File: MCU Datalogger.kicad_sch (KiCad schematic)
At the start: 0 parts

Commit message: Added required symbols to the schematic sheets.
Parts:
- added BT1: Battery, Connector_PinHeader_2.54mm:PinHeader_1x02_P2.54mm_Vertical, symbol Device:Battery
- added C1, C4: 0.1uF, Capacitor_SMD:C_0805_2012Metric, symbol Device:C
- added C2, C3: 22pF, Capacitor_SMD:C_0805_2012Metric, symbol Device:C
- added C5: 100nF, Capacitor_SMD:C_0805_2012Metric, symbol Device:C
- added D1, D2: LED, LED_SMD:LED_0805_2012Metric, symbol Device:LED
- added H1, H2, H3, H4: MountingHole, MountingHole:MountingHole_2.1mm, symbol Mechanical:MountingHole
- added J1, J3: Conn_01x04_Pin, Connector_PinHeader_2.54mm:PinHeader_1x04_P2.54mm_Vertical, symbol Connector:Conn_01x04_Pin
- added J2: Conn_01x09_Pin, Connector_PinHeader_2.54mm:PinHeader_1x09_P2.54mm_Vertical, symbol Connector:Conn_01x09_Pin
- added J4: Conn_02x03_Odd_Even, Connector_PinHeader_2.54mm:PinHeader_2x03_P2.54mm_Vertical, symbol Connector_Generic:Conn_02x03_Odd_Even
- added R1, R2, R6: 10K, Resistor_SMD:R_0805_2012Metric, symbol Device:R
- added R3, R4: 4.7K, Resistor_SMD:R_0805_2012Metric, symbol Device:R
- added R5, R7: 330, Resistor_SMD:R_0805_2012Metric, symbol Device:R
- added U1: DS1337S_, DS1337S_:SOIC127P600X175-8N, symbol DS1337S_:DS1337S_
- added U2, U3: 24LC1025, Package_SO:SOIC-8_5.3x5.3mm_P1.27mm, symbol Memory_EEPROM:24LC1025
- added U4: ATMEGA328P-AU, ATMEGA328P-AU:QFP80P900X900X120-32N, symbol ATMEGA328P-AU:ATMEGA328P-AU
- added Y1: 32.768 KHz, Crystal:Crystal_SMD_5032-2Pin_5.0x3.2mm_HandSoldering, symbol Device:Crystal
- added Y2: 16 MHz, Crystal:Crystal_SMD_5032-2Pin_5.0x3.2mm_HandSoldering, symbol Device:Crystal
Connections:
- new net GND: U4.21 (GND), U4.3 (GND), U4.5 (GND)
- new net VCC: U4.4 (VCC), U4.6 (VCC)
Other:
- title: (none) -> MCU Datalogger

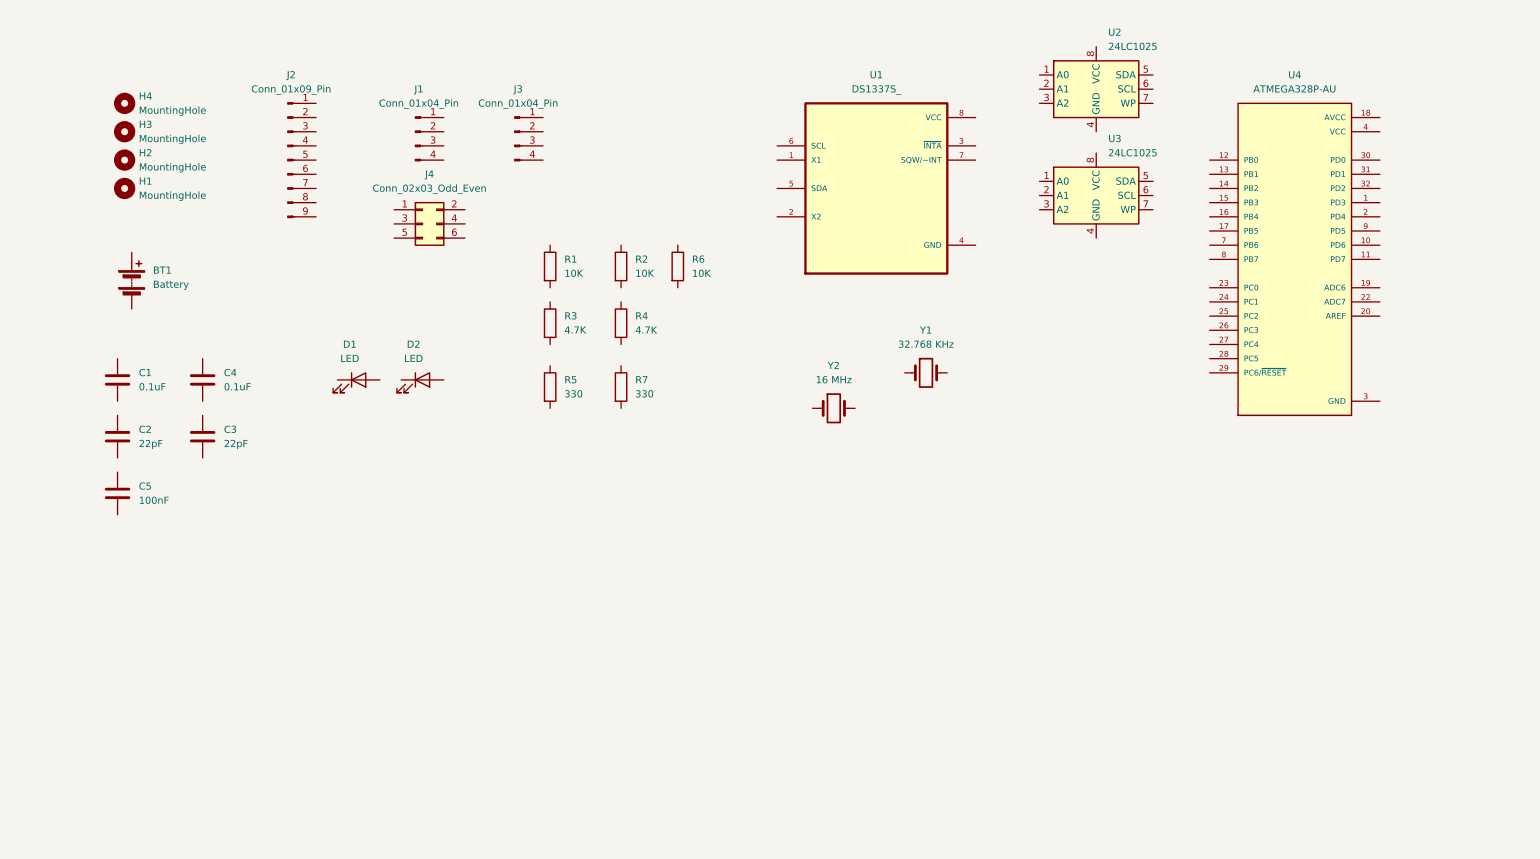
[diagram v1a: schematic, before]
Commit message: Completed wiring of main sheet.
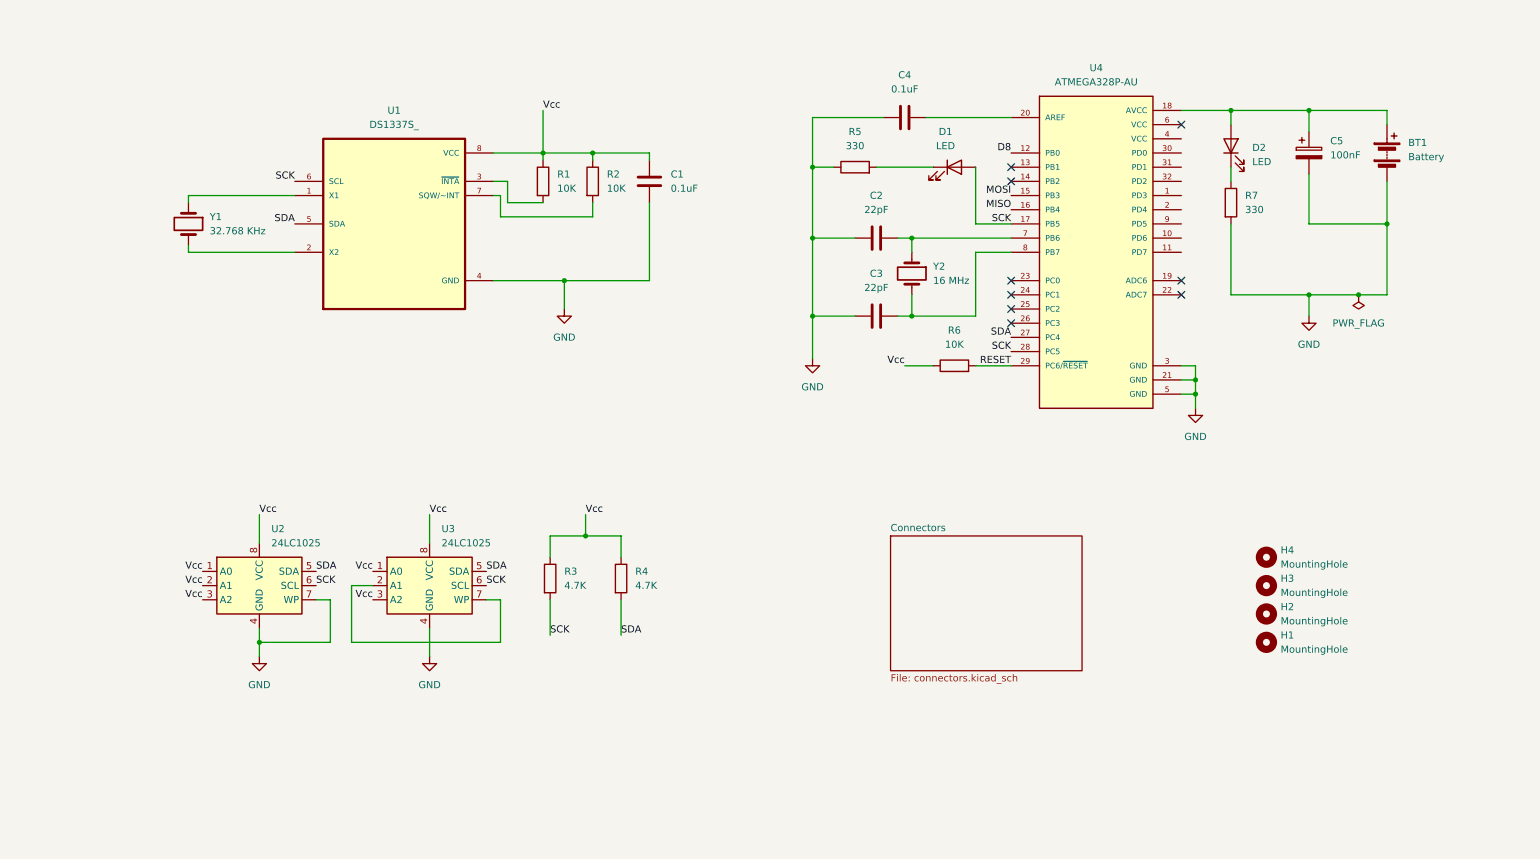
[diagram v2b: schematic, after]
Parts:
- removed J1, J3: Conn_01x04_Pin, Connector_PinHeader_2.54mm:PinHeader_1x04_P2.54mm_Vertical, symbol Connector:Conn_01x04_Pin
- removed J2: Conn_01x09_Pin, Connector_PinHeader_2.54mm:PinHeader_1x09_P2.54mm_Vertical, symbol Connector:Conn_01x09_Pin
- removed J4: Conn_02x03_Odd_Even, Connector_PinHeader_2.54mm:PinHeader_2x03_P2.54mm_Vertical, symbol Connector_Generic:Conn_02x03_Odd_Even
- C5: symbol Device:C -> Device:C_Polarized
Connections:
- net GND: now also BT1.2 (-), C1.2, C2.2, C3.2, C4.1, C5.2, R5.1, R7.2, U1.4 (GND), U2.4 (GND), U2.7 (WP), U3.4 (GND)
- net at R4.1: no longer names the net of R4.1
- net at R4.1: now also C1.1, R1.1, R2.1, R3.1, R6.1, U1.8 (VCC), U2.1 (A0), U2.2 (A1), U2.3 (A2), U2.8 (VCC), U3.1 (A0), U3.3 (A2), U3.8 (VCC)
- net SDA: now reaches R4.2
- net SDA: now also U1.5 (SDA), U2.5 (SDA), U3.5 (SDA), U4.27 (PC4)
- net at Y1.1: now also U1.1 (X1)
- net at Y1.2: now also U1.2 (X2)
- net RESET: now reaches R6.2
- net RESET: now also U4.29 (PC6/~{RESET})
- net at R5.2: now also D1.1 (K)
- net at R1.2: now also U1.3 (~{INTA})
- net at BT1.1 (+): now also C5.1, D2.2 (A), U4.18 (AVCC)
- net SCK: now reaches U1.6 (SCL)
- net SCK: now also D1.2 (A), R3.2, U2.6 (SCL), U3.6 (SCL), U4.17 (PB5), U4.28 (PC5)
- net at U1.7 (SQW/~INT): now also R2.2
- net at D2.1 (K): now also R7.1
- net at C3.1: now also U4.8 (PB7), Y2.2
- net at C2.1: now also U4.7 (PB6), Y2.1
- net at U3.2 (A1): now also U3.7 (WP)
- net at C4.2: now also U4.20 (AREF)
- net D8: now reaches U4.12 (PB0)
- net MOSI: now reaches U4.15 (PB3)
- net MISO: now reaches U4.16 (PB4)
- net VCC: no longer names the net of U4.4 (VCC)
- net VCC: no longer U4.6 (VCC)
- no-connect marks 0 -> 9
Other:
- added sheet Connectors (connectors.kicad_sch)
- moved on the sheet: BT1, C1, C2, C3, C4, D1, D2, H1, H2, H3, H4, R1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

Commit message: Update setup for schematic editor.
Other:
- title: MCU Datalogger -> ${project_name}
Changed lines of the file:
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@@
 	(paper "A4")
 	(title_block
-		(title "MCU Datalogger")
+		(title "${project_name}")
 		(date "2026-04-26")
 		(rev "1")

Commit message: Completed schematic editor
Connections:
- net Vcc: now reaches C1.1, R1.1, R2.1, R3.1, R4.1, R6.1, U1.8 (VCC), U2.1 (A0), U2.2 (A1), U2.3 (A2), U2.8 (VCC), U3.1 (A0), U3.3 (A2), U3.8 (VCC)
- net Vcc: now also BT1.1 (+), C5.1, D2.2 (A), U4.18 (AVCC), U4.4 (VCC)
- net D3: now reaches U4.1 (PD3)
- net D6: now reaches U4.10 (PD6)
- net D7: now reaches U4.11 (PD7)
- net D4: now reaches U4.2 (PD4)
- net RX: now reaches U4.30 (PD0)
- net TX: now reaches U4.31 (PD1)
- net D2: now reaches U4.32 (PD2)
- net D5: now reaches U4.9 (PD5)
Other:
- sheet Connectors ports: added D2, D3, D4, D5, D6, D7, D8, GND, MISO, MOSI, RESET, RX, SCK, SDA, TX, Vcc; removed none
- note added: "EEPROM"
- note added: "MCU"
- note added: "Mounting Hole"
- note added: "Real-time Clock"
- moved on the sheet: BT1, C1, C2, C3, C4, C5, D1, D2, H1, H2, H3, H4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
